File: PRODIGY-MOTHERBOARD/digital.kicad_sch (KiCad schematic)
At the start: 75 parts, among them Q2 BC850, Q3 BS870, Q4 BC850, SW3 SW_Push, SW4 SW_Push, SW5 SW_Push, SW6 SW_Push, U18 SN74LVC1T45DBV, U19 TSOP4836

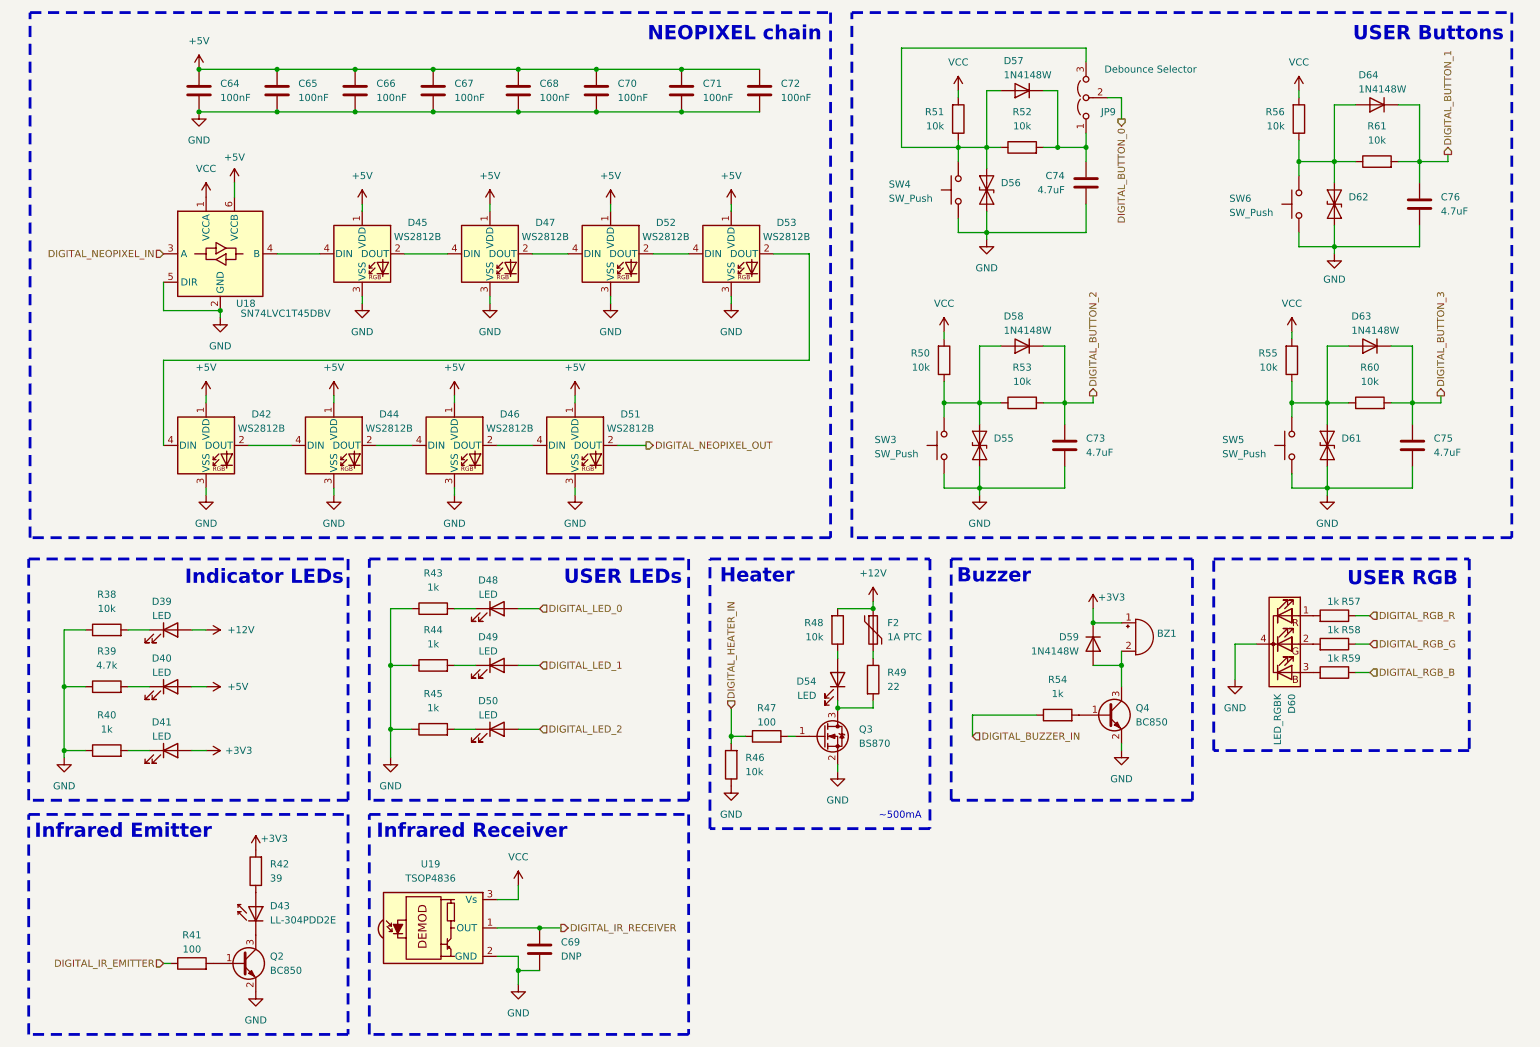
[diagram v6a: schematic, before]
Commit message: finished motherboard bom and updated footprints
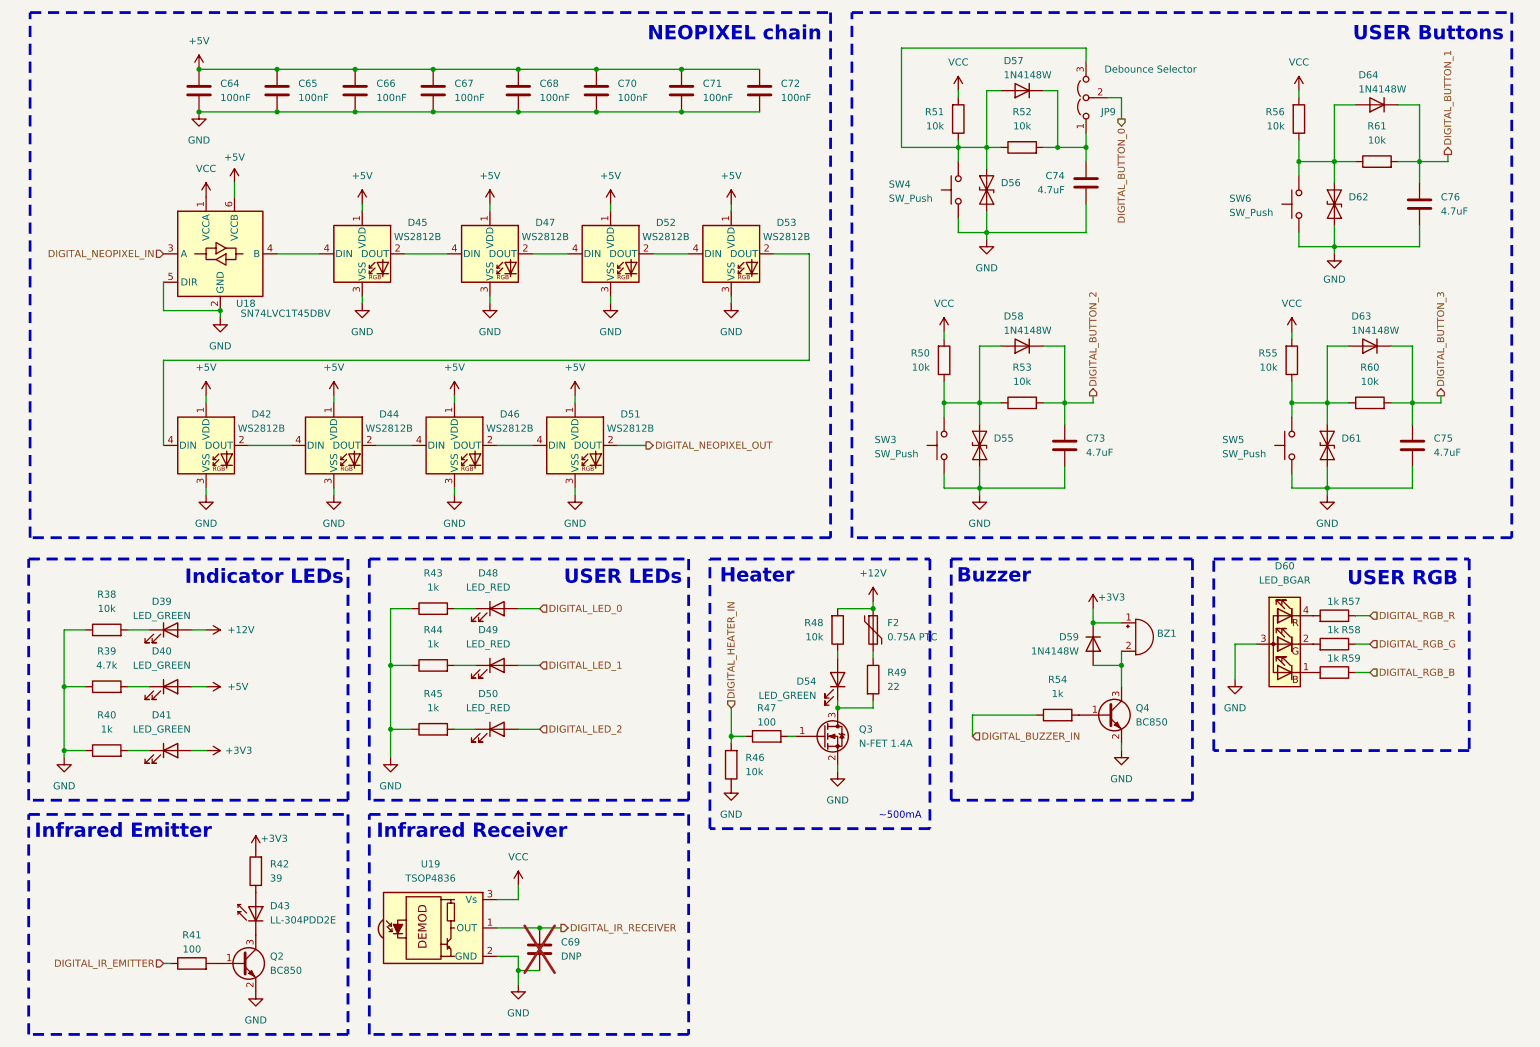
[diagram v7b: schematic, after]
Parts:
- removed D60: LED_RGBK, LED_THT:LED_D5.0mm-4_RGB, symbol Device:LED_RGBK
- added D60: LED_BGAR, LED_THT:LED_D5.0mm-4_RGB, symbol Device:LED_BGAR
- C64, C65, C66, C67, C68, C70, C71, C72: TME (none) -> CL10B104KB8NNNC
- C69: now not fitted
- C73, C74, C75, C76: TME (none) -> CL21A475KAQNNNG
- D39, D40, D41, D54: value LED -> LED_GREEN; footprint LED_THT:LED_D5.0mm -> LED_THT:LED_D3.0mm; TME (none) -> L-934LGD
- D42, D44, D45, D46, D47, D51, D52, D53: TME (none) -> WS2812B-V5
- D43: TME (none) -> LL-304PDD2E
- D48, D49, D50: value LED -> LED_RED; footprint LED_THT:LED_D5.0mm -> LED_THT:LED_D3.0mm; TME (none) -> L-934ID
- D55, D56, D61, D62: TME (none) -> SD05.TCT
- D57, D58, D59, D63, D64: footprint Diode_SMD:D_SOD-123 -> Diode_SMD:D_SOD-323; TME (none) -> 1N4148WSTR-SMC
- F2: value 1A PTC -> 0.75A PTC; TME (none) -> 0ZCG0075FF2C
- JP9: TME (none) -> JUMPER-H/R
- Q2, Q4: TME (none) -> BC850B-DIO
- Q3: value BS870 -> N-FET 1.4A; TME (none) -> BSS316NH6327XTSA1
- R38, R46, R48, R50, R51, R52, R53, R55, R56, R60, R61: TME (none) -> WR06X1002FTL
- R39: TME (none) -> CRCW06034K70FKTABC
- R40, R43, R44, R45, R54, R57, R58, R59: TME (none) -> RC0603JR-071K
- R41, R47: TME (none) -> SMD0603-100R
- R42: TME (none) -> AR0805-39R-0.1%
- R49: TME (none) -> CRCW251222R0FKTHBC
- SW3, SW4, SW5, SW6: footprint Button_Switch_SMD:SW_Push_1P1T_NO_6x6mm_H9.5mm -> Button_Switch_SMD:SW_SPST_Omron_B3FS-105xP; TME (none) -> B3FS-1050
- U18: TME (none) -> SN74LVC1T45DBVR
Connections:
- net GND: now also D60.3 (A)
- net at R57.2: now also D60.4 (RK)
- net at R59.2: now also D60.1 (BK)
- net at R58.2: now also D60.2 (GK)
